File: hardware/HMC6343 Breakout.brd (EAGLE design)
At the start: 20.3 x 20.3 mm, 15 parts, among them U1 HMC6343A

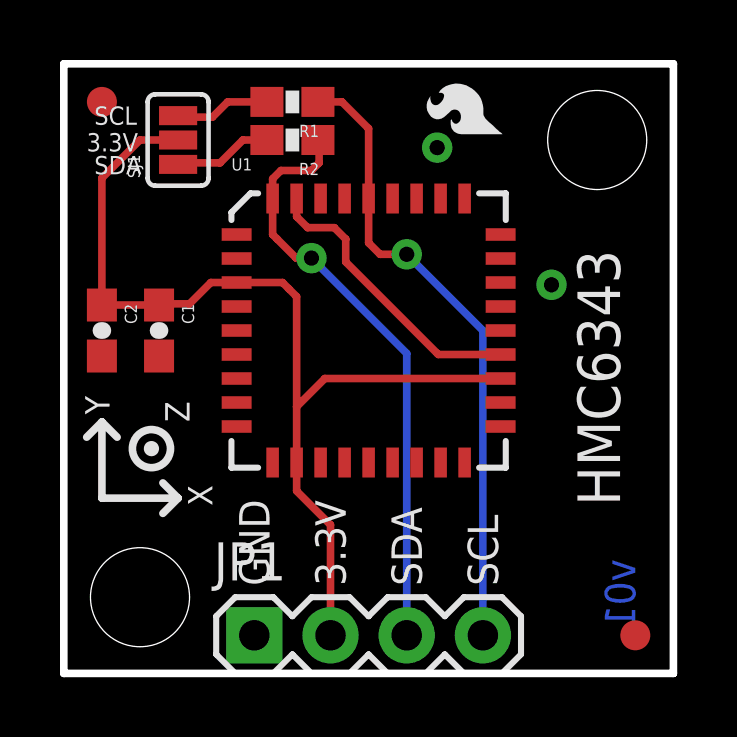
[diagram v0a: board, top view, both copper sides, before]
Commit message: v01 updated based on review feedback
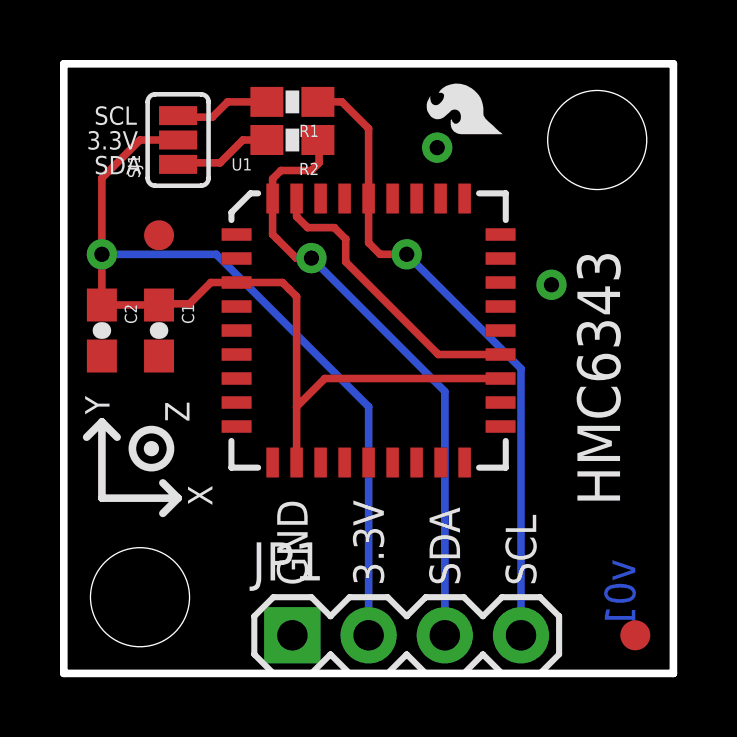
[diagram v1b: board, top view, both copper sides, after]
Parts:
- moved FID2 4.84 mm to (3.17, 14.6)
- moved JP1 1.27 mm to (7.62, 1.27)
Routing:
- net 3.3V: track 33.3 -> 45.6 mm, vias 0 -> 1
- net SDA: track 19.9 -> 20.4 mm
- net SCL: track 21.0 -> 21.6 mm
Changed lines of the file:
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@@
 <wire x1="20.32" y1="20.32" x2="0" y2="20.32" width="0.254" layer="20"/>
 <wire x1="0" y1="20.32" x2="0" y2="0" width="0.254" layer="20"/>
-<text x="6.858" y="2.921" size="1.016" layer="21" font="vector" ratio="15" rot="R90">GND</text>
-<text x="9.398" y="2.921" size="1.016" layer="21" font="vector" ratio="15" rot="R90">3.3V</text>
-<text x="11.938" y="2.921" size="1.016" layer="21" font="vector" ratio="15" rot="R90">SDA</text>
-<text x="14.478" y="2.921" size="1.016" layer="21" font="vector" ratio="15" rot="R90">SCL</text>
+<text x="8.128" y="2.921" size="1.016" layer="21" font="vector" ratio="15" rot="R90">GND</text>
+<text x="10.668" y="2.921" size="1.016" layer="21" font="vector" ratio="15" rot="R90">3.3V</text>
+<text x="13.208" y="2.921" size="1.016" layer="21" font="vector" ratio="15" rot="R90">SDA</text>
+<text x="15.748" y="2.921" size="1.016" layer="21" font="vector" ratio="15" rot="R90">SCL</text>
 <wire x1="1.27" y1="5.842" x2="1.27" y2="8.382" width="0.254" layer="21"/>
 <wire x1="1.27" y1="5.842" x2="3.81" y2="5.842" width="0.254" layer="21"/>
@@
 <text x="4.191" y="8.382" size="0.8128" layer="21" font="vector" ratio="15" rot="R90">Z</text>
 <text x="1.016" y="16.637" size="0.6096" layer="21" font="vector" ratio="15">SDA</text>
-<text x="0.762" y="17.399" size="0.6096" layer="21" font="vector" ratio="15">3.3V</text>
+<text x="0.762" y="17.4625" size="0.6096" layer="21" font="vector" ratio="15">3.3V</text>
 <text x="1.016" y="18.288" size="0.6096" layer="21" font="vector" ratio="15">SCL</text>
 <text x="18.542" y="5.588" size="1.4224" layer="21" font="vector" ratio="15" rot="R90">HMC6343</text>
@@
 <text x="14.986" y="13.462" size="1.016" layer="22" font="vector" ratio="15" rot="SMR270">Breakout</text>
 <text x="19.05" y="3.81" size="1.016" layer="16" font="vector" ratio="15" rot="SMR270">v01</text>
+<wire x1="1.397" y1="16.256" x2="1.397" y2="18.796" width="0.254" layer="22"/>
+<wire x1="1.397" y1="16.256" x2="3.937" y2="16.256" width="0.254" layer="22"/>
+<wire x1="1.397" y1="18.796" x2="0.889" y2="18.288" width="0.254" layer="22"/>
+<wire x1="1.397" y1="18.796" x2="1.905" y2="18.288" width="0.254" layer="22"/>
+<wire x1="3.937" y1="16.256" x2="3.429" y2="16.764" width="0.254" layer="22"/>
+<wire x1="3.937" y1="16.256" x2="3.429" y2="15.748" width="0.254" layer="22"/>
+<circle x="2.921" y="17.78" radius="0.635" width="0.254" layer="22"/>
+<text x="5.08" y="16.5481" size="0.8128" layer="22" font="vector" ratio="15" rot="SMR270">X</text>
+<text x="1.651" y="19.6215" size="0.8128" layer="22" font="vector" ratio="15" rot="SMR270">Y</text>
+<text x="4.445" y="19.05" size="0.8128" layer="22" font="vector" ratio="15" rot="SMR270">Z</text>
+<wire x1="3.175" y1="18.034" x2="2.667" y2="17.526" width="0.254" layer="22"/>
+<wire x1="2.667" y1="18.034" x2="3.175" y2="17.526" width="0.254" layer="22"/>
 </plain>
 <attributes>
@@
 <element name="U1" library="SparkFun-Sensors" package="LCC36" value="HMC6343A" x="10.16" y="11.43"/>
 <element name="SJ1" library="SparkFun-Passives" package="SJ_3_PASTE1&amp;2&amp;3" value="" x="3.81" y="17.78" rot="R90"/>
-<element name="JP1" library="SparkFun-Connectors" package="1X04" value="" x="6.35" y="1.27"/>
+<element name="JP1" library="SparkFun-Connectors" package="1X04" value="" x="7.62" y="1.27"/>
 <element name="C1" library="SparkFun-Capacitors" package="0603-CAP" value="0.1uF" x="3.175" y="11.43" rot="R270">
 <attribute name="PROD_ID" value="CAP-00810" x="-20.955" y="-27.94" size="1.778" layer="27" rot="R270" display="off"/>
@@
 </element>
 <element name="FID1" library="SparkFun-Aesthetics" package="FIDUCIAL-1X2" value="FIDUCIAL1X2" x="19.05" y="1.27"/>
-<element name="FID2" library="SparkFun-Aesthetics" package="FIDUCIAL-1X2" value="FIDUCIAL1X2" x="1.27" y="19.05"/>
+<element name="FID2" library="SparkFun-Aesthetics" package="FIDUCIAL-1X2" value="FIDUCIAL1X2" x="3.175" y="14.605"/>
 <element name="STANDOFF1" library="SparkFun-Electromechanical" package="STAND-OFF" value="STAND-OFF" x="17.78" y="17.78"/>
 <element name="STANDOFF2" library="SparkFun-Electromechanical" package="STAND-OFF" value="STAND-OFF" x="2.54" y="2.54"/>
@@
 <contactref element="JP1" pad="2"/>
 <contactref element="SJ1" pad="2"/>
-<wire x1="8.89" y1="1.27" x2="8.89" y2="4.953" width="0.254" layer="1"/>
 <wire x1="7.747" y1="7.017" x2="7.76" y2="7.03" width="0.254" layer="1"/>
-<wire x1="7.76" y1="7.03" x2="7.76" y2="6.083" width="0.254" layer="1"/>
-<wire x1="7.76" y1="6.083" x2="8.89" y2="4.953" width="0.254" layer="1"/>
 <wire x1="1.27" y1="12.28" x2="3.175" y2="12.28" width="0.254" layer="1"/>
 <wire x1="5.76" y1="13.03" x2="4.902" y2="13.03" width="0.254" layer="1"/>
@@
 <wire x1="3.81" y1="17.78" x2="2.54" y2="17.78" width="0.254" layer="1"/>
 <wire x1="2.54" y1="17.78" x2="1.27" y2="16.51" width="0.254" layer="1"/>
-<wire x1="1.27" y1="16.51" x2="1.27" y2="12.28" width="0.254" layer="1"/>
+<wire x1="10.16" y1="1.27" x2="10.16" y2="8.89" width="0.254" layer="16"/>
+<wire x1="10.16" y1="8.89" x2="5.08" y2="13.97" width="0.254" layer="16"/>
+<wire x1="5.08" y1="13.97" x2="1.27" y2="13.97" width="0.254" layer="16"/>
+<via x="1.27" y="13.97" extent="1-16" drill="0.508"/>
+<wire x1="1.27" y1="13.97" x2="1.27" y2="12.28" width="0.254" layer="1"/>
+<wire x1="1.27" y1="16.51" x2="1.27" y2="13.97" width="0.254" layer="1"/>
 </signal>
 <signal name="N$1">
@@
 <wire x1="9.271" y1="19.05" x2="10.16" y2="18.161" width="0.254" layer="1"/>
 <wire x1="10.16" y1="18.161" x2="10.16" y2="15.83" width="0.254" layer="1"/>
-<wire x1="13.97" y1="1.27" x2="13.97" y2="11.43" width="0.254" layer="16"/>
-<wire x1="13.97" y1="11.43" x2="11.43" y2="13.97" width="0.254" layer="16"/>
+<wire x1="15.24" y1="1.27" x2="15.24" y2="10.16" width="0.254" layer="16"/>
+<wire x1="15.24" y1="10.16" x2="11.43" y2="13.97" width="0.254" layer="16"/>
 <via x="11.43" y="13.97" extent="1-16" drill="0.508"/>
 <wire x1="11.43" y1="13.97" x2="10.541" y2="13.97" width="0.254" layer="1"/>
@@
 <wire x1="8.509" y1="17.018" x2="8.509" y2="17.741" width="0.254" layer="1"/>
 <wire x1="8.509" y1="17.741" x2="8.47" y2="17.78" width="0.254" layer="1"/>
-<wire x1="11.43" y1="1.27" x2="11.43" y2="10.668" width="0.254" layer="16"/>
-<wire x1="11.43" y1="10.668" x2="8.255" y2="13.843" width="0.254" layer="16"/>
+<wire x1="12.7" y1="1.27" x2="12.7" y2="9.398" width="0.254" layer="16"/>
+<wire x1="12.7" y1="9.398" x2="8.255" y2="13.843" width="0.254" layer="16"/>
 <via x="8.255" y="13.843" extent="1-16" drill="0.508"/>
 <wire x1="8.255" y1="13.843" x2="7.747" y2="13.843" width="0.254" layer="1"/>

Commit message: v10, ready for reds
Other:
- board text added: "v10"
- board text removed: "v01"
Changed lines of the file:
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@@
 <text x="13.335" y="15.24" size="1.016" layer="22" font="vector" ratio="15" rot="SMR270">Magnetometer</text>
 <text x="14.986" y="13.462" size="1.016" layer="22" font="vector" ratio="15" rot="SMR270">Breakout</text>
-<text x="19.05" y="3.81" size="1.016" layer="16" font="vector" ratio="15" rot="SMR270">v01</text>
+<text x="19.05" y="3.81" size="1.016" layer="16" font="vector" ratio="15" rot="SMR270">v10</text>
 <wire x1="1.397" y1="16.256" x2="1.397" y2="18.796" width="0.254" layer="22"/>
 <wire x1="1.397" y1="16.256" x2="3.937" y2="16.256" width="0.254" layer="22"/>
